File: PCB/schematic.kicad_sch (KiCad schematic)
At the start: 8 parts, among them J1 Conn_01x04, SW1 SW_Push, SW2 SW_Push, SW3 SW_Push, SW4 RotaryEncoder_Switch, U1 MOUDLE-SEEEDUINO-XIAO

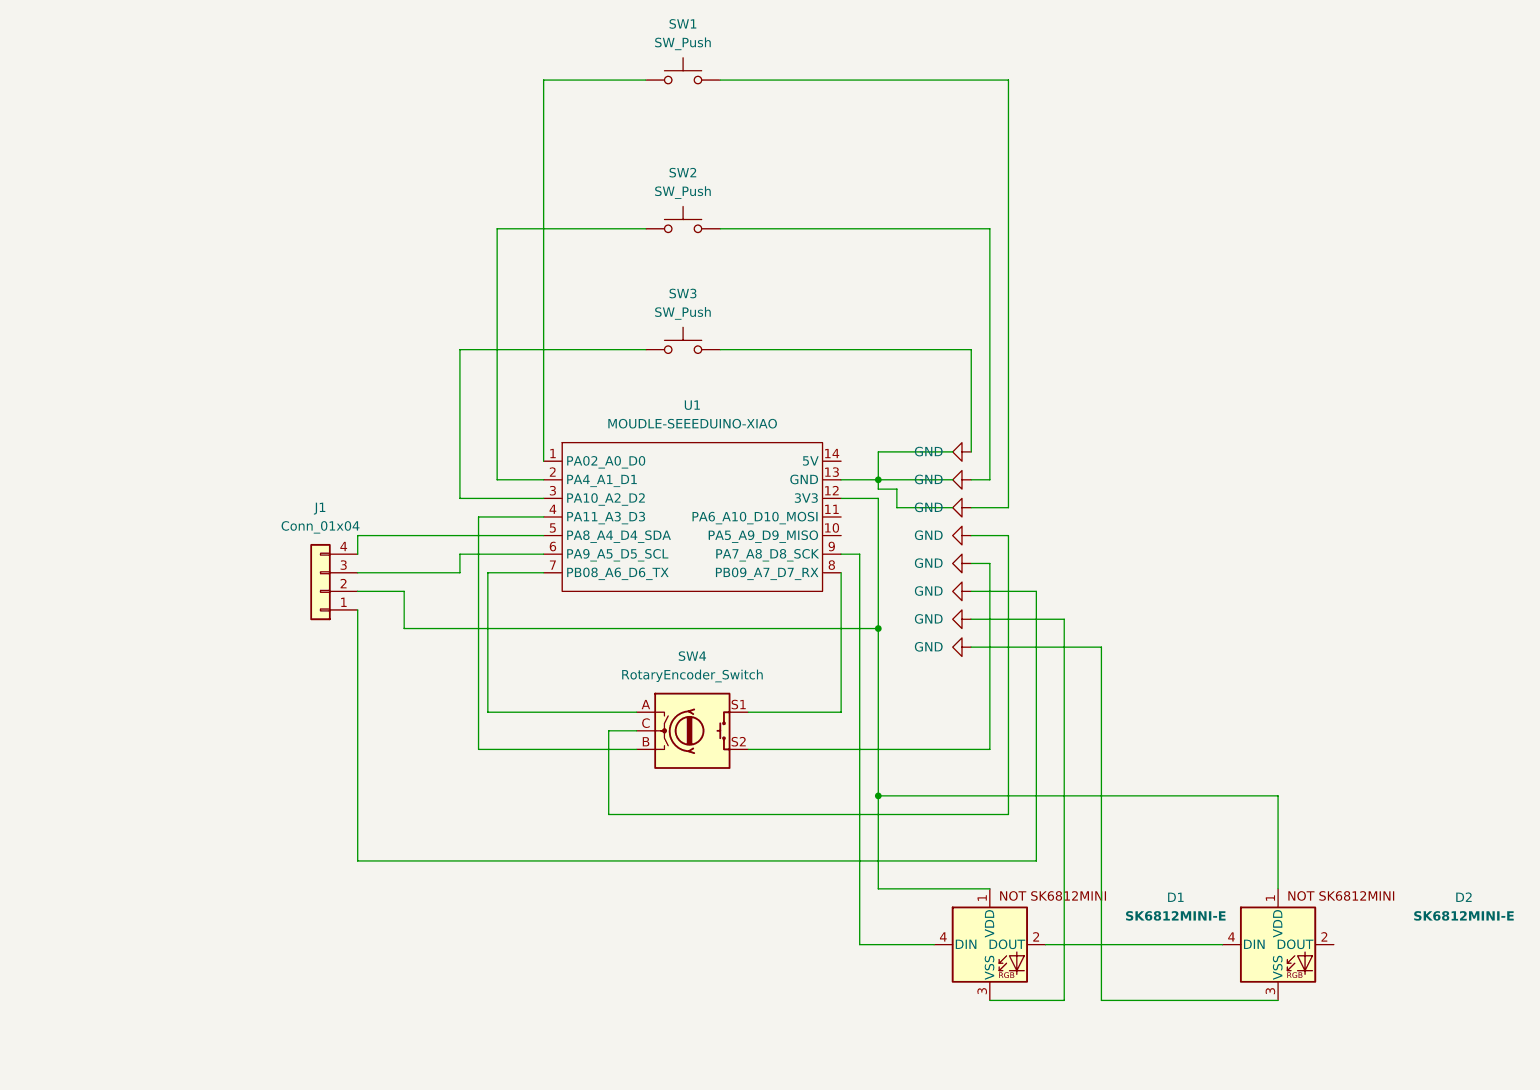
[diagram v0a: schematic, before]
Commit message: Complete revamp of the 3d models due to precision mistakes repaired using 3d models of mechanical parts. Minor chnages to readme.
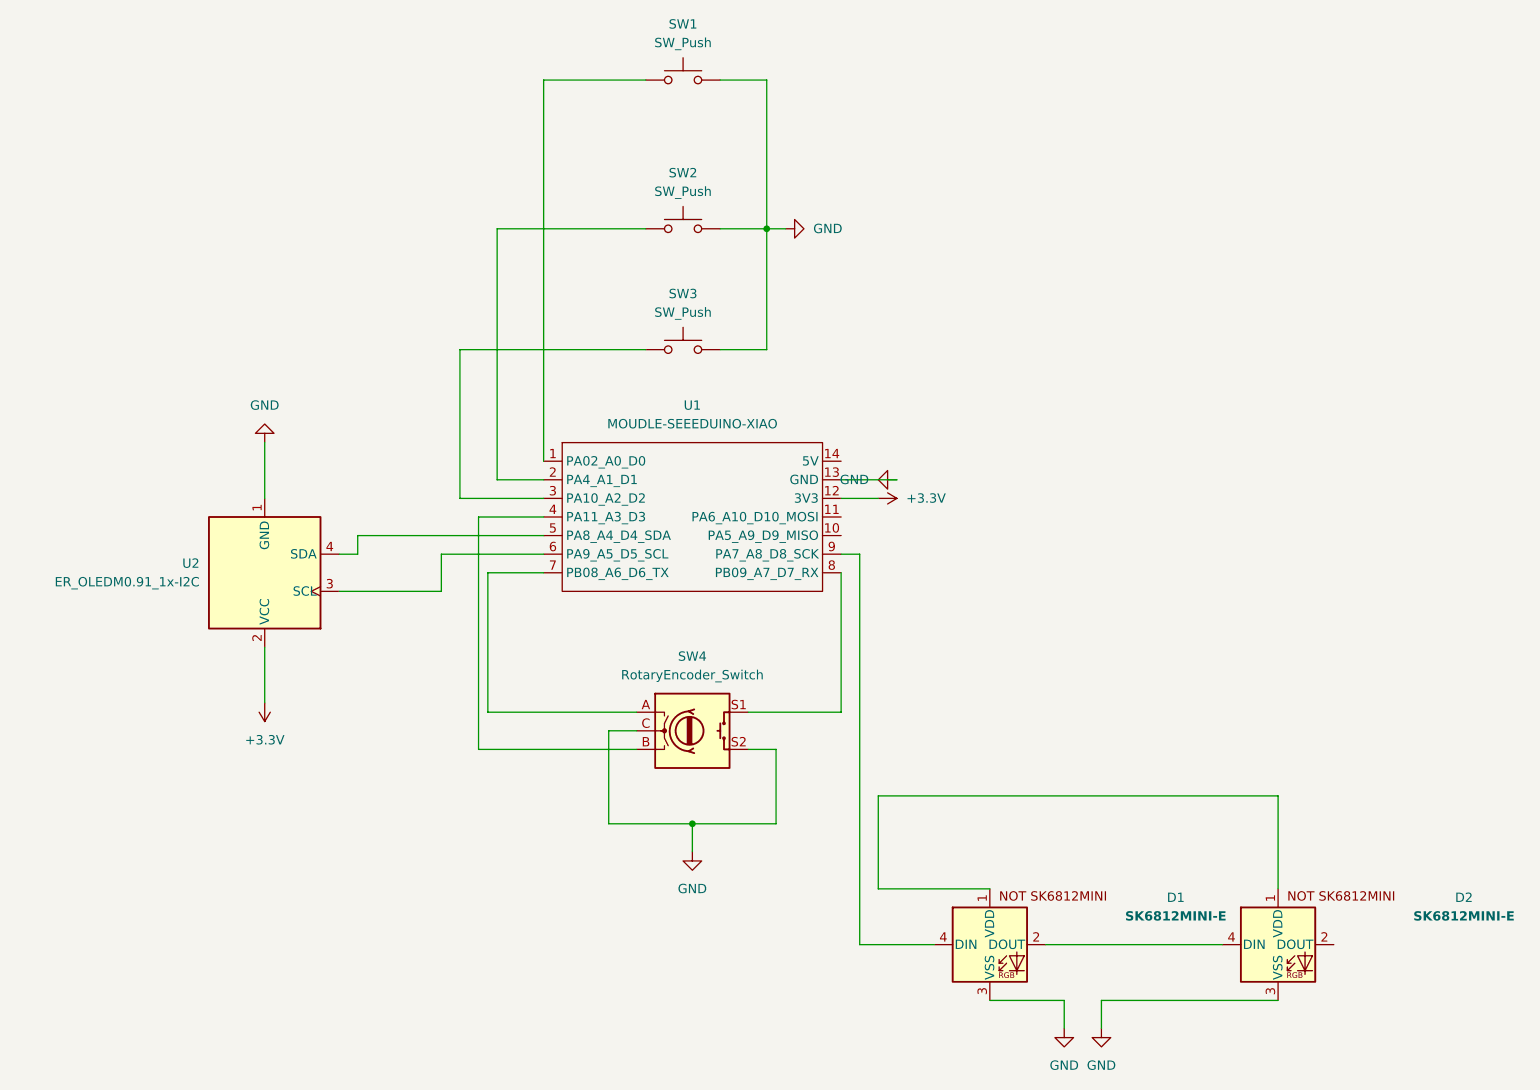
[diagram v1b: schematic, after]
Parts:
- removed J1: Conn_01x04, symbol Connector_Generic:Conn_01x04
- added U2: ER_OLEDM0.91_1x-I2C, Display:ER_OLEDM0.91_1x-I2C, symbol Display_Graphic:ER_OLEDM0.91_1x-I2C
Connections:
- net GND: now also U1.13 (GND), U2.1 (GND)
- net at D1.1 (VDD), D2.1 (VDD): no longer U1.12 (3V3)
- net at U1.6 (PA9_A5_D5_SCL): now also U2.3 (SCL)
- net at U1.5 (PA8_A4_D4_SDA): now also U2.4 (SDA)
- new net +3.3V: U1.12 (3V3), U2.2 (VCC)
